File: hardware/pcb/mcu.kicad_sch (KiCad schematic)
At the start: 35 parts, among them J1 Conn_01x05, J2 Conn_01x06, Q1 BC817, SW2 SW_Push, SW3 SW_Push, U2 STM32F411CEU6, U4 PCF8574AP, Y1 8MHz Crystal, Y2 32.768 kHz Crystal

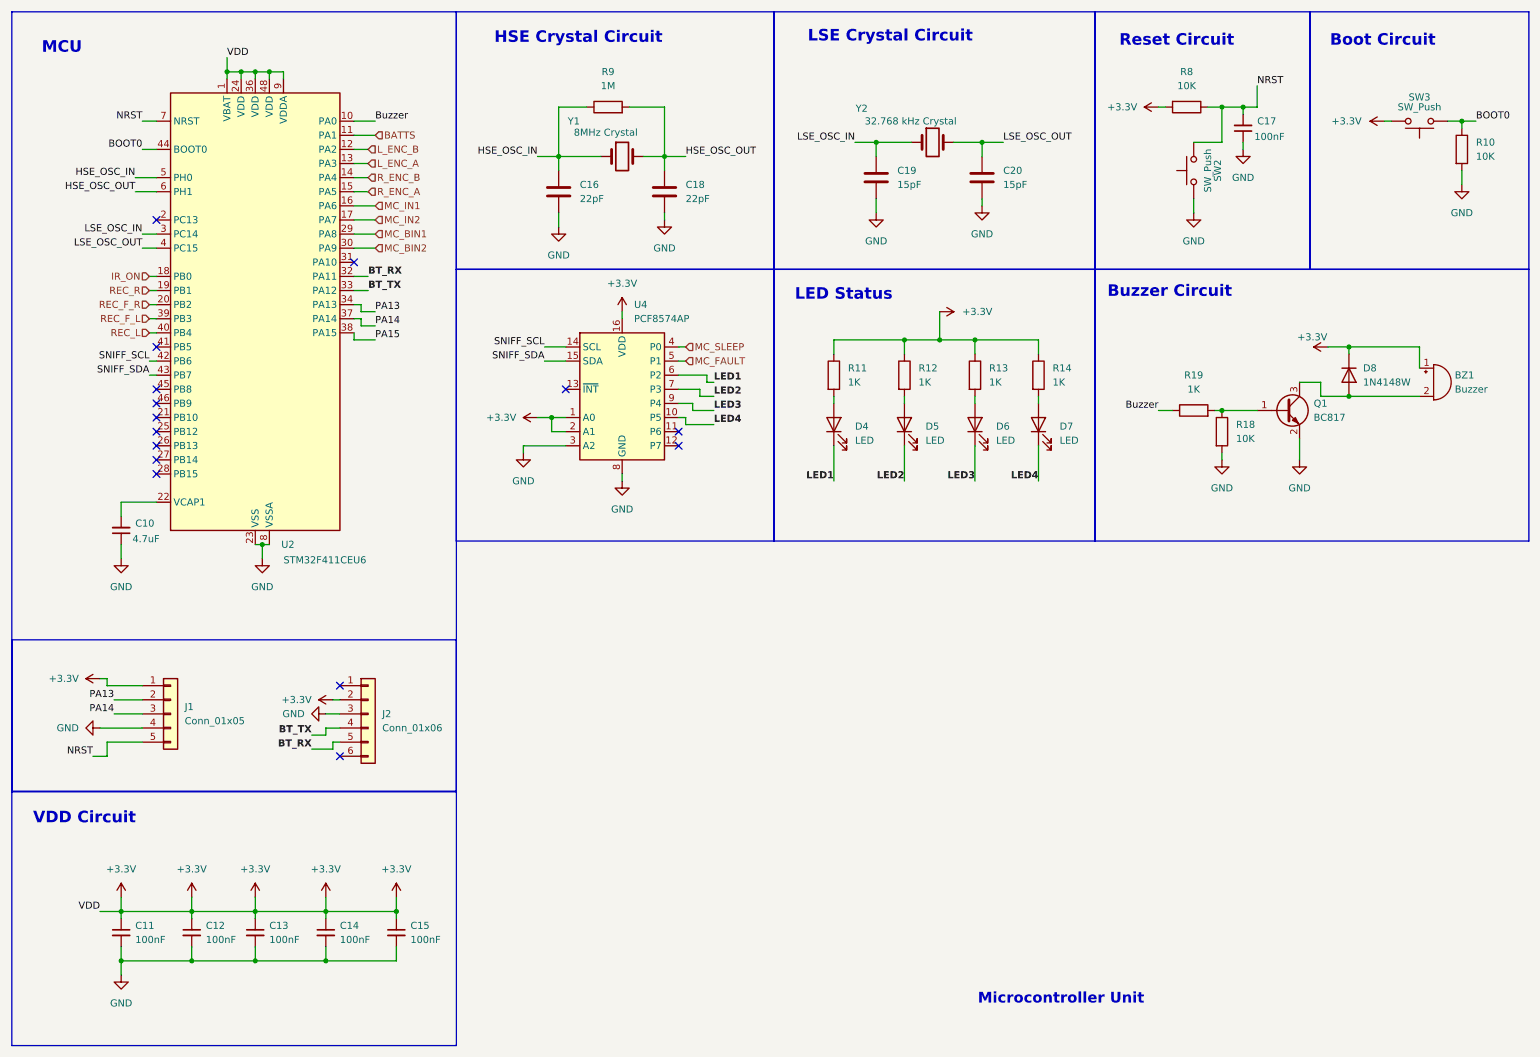
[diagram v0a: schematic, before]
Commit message: hardware: freeze schematic v1 after complete PCB redesign
Complete PCB and schematic refresh with reorganized sheets (psu, ui),
updated MCU/motor/sensor subsystems, and v1 schematic baseline frozen.
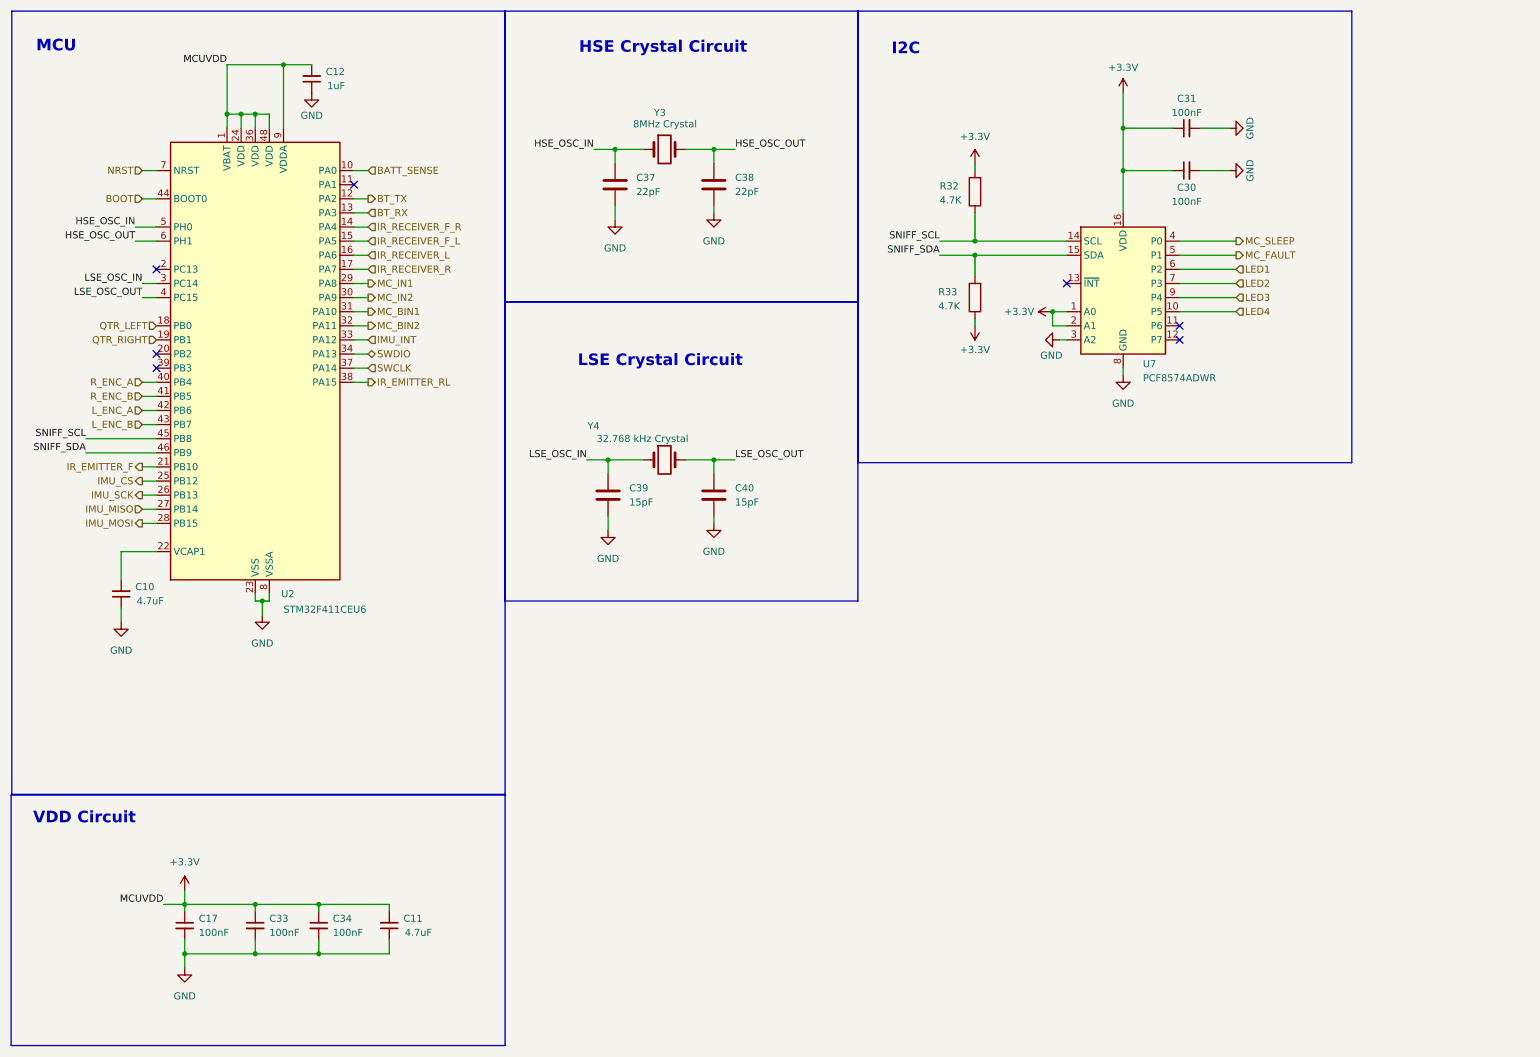
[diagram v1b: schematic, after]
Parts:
- removed BZ1: Buzzer, Buzzer_Beeper:Buzzer_Murata_PKMCS0909E, symbol Device:Buzzer
- removed C13, C14, C15: 100nF, Capacitor_SMD:C_0805_2012Metric_Pad1.18x1.45mm_HandSolder, symbol Device:C_Small
- removed C16, C18: 22pF, Capacitor_SMD:C_0603_1608Metric_Pad1.08x0.95mm_HandSolder, symbol Device:C
- removed C19, C20: 15pF, Capacitor_SMD:C_0603_1608Metric_Pad1.08x0.95mm_HandSolder, symbol Device:C
- removed D4, D5, D6, D7: LED, LED_SMD:LED_0805_2012Metric_Pad1.15x1.40mm_HandSolder, symbol Device:LED
- removed D8: 1N4148W, Diode_SMD:D_SOD-123, symbol Diode:1N4148W
- removed J1: Conn_01x05, Connector_PinHeader_1.00mm:PinHeader_1x05_P1.00mm_Vertical, symbol Connector_Generic:Conn_01x05
- removed J2: Conn_01x06, Connector_PinHeader_1.00mm:PinHeader_1x06_P1.00mm_Vertical, symbol Connector_Generic:Conn_01x06
- removed Q1: BC817, Package_TO_SOT_SMD:SOT-23, symbol Transistor_BJT:BC817
- removed R10, R18, R8: 10K, Resistor_SMD:R_0805_2012Metric_Pad1.20x1.40mm_HandSolder, symbol Device:R
- removed R11, R12, R13, R14, R19: 1K, Resistor_SMD:R_0805_2012Metric_Pad1.20x1.40mm_HandSolder, symbol Device:R
- removed R9: 1M, Resistor_SMD:R_0603_1608Metric_Pad0.98x0.95mm_HandSolder, symbol Device:R
- removed SW2, SW3: SW_Push, Button_Switch_SMD:SW_SPST_B3U-3000P, symbol Switch:SW_Push
- removed U4: PCF8574AP, Package_SO:TSSOP-16_4.4x5mm_P0.65mm, symbol Interface_Expansion:PCF8574AP
- removed Y1: 8MHz Crystal, Crystal:Crystal_SMD_3225-4Pin_3.2x2.5mm_HandSoldering, symbol Device:Crystal
- removed Y2: 32.768 kHz Crystal, Crystal:Crystal_SMD_3225-4Pin_3.2x2.5mm_HandSoldering, symbol Device:Crystal
- added C30, C31, C33, C34: 100nF, Capacitor_SMD:C_0805_2012Metric_Pad1.18x1.45mm_HandSolder, symbol Device:C_Small
- added C37, C38: 22pF, Capacitor_SMD:C_0603_1608Metric_Pad1.08x0.95mm_HandSolder, symbol Device:C
- added C39, C40: 15pF, Capacitor_SMD:C_0603_1608Metric_Pad1.08x0.95mm_HandSolder, symbol Device:C
- added R32, R33: 4.7K, Resistor_SMD:R_0805_2012Metric_Pad1.20x1.40mm_HandSolder, symbol Device:R
- added U7: PCF8574ADWR, Package_SO:SOIC-16W_7.5x10.3mm_P1.27mm, symbol Interface_Expansion:PCF8574AP
- added Y3: 8MHz Crystal, Crystal:Crystal_SMD_3225-4Pin_3.2x2.5mm_HandSoldering, symbol Device:Crystal
- added Y4: 32.768 kHz Crystal, Crystal:Crystal_SMD_3225-4Pin_3.2x2.5mm_HandSoldering, symbol Device:Crystal
- C11: value 100nF -> 4.7uF
- C12: value 100nF -> 1uF
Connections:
- net REC_L is gone; now on net R_ENC_A: U2.40 (PB4)
- net +3.3V: now also C11.2, C12.2, C17.1, C30.1, C31.1, C33.1, C34.1, R32.2, R33.1, U7.1 (A0), U7.16 (VDD), U7.2 (A1); no longer C11.1, C12.1
- net BT_RX: now also U2.13 (PA3); no longer U2.32 (PA11)
- net BT_TX: now also U2.12 (PA2); no longer U2.33 (PA12)
- net GND: now also C11.1, C12.1, C17.2, C30.2, C31.2, C33.2, C34.2, C37.2, C38.2, C39.2, C40.2, U7.3 (A2), U7.8 (GND); no longer C11.2, C12.2, C17.1
- net HSE_OSC_IN: now also C37.1, Y3.1
- net HSE_OSC_OUT: now also C38.1, Y3.2
- net LED1: now also U7.6 (P2)
- net LED2: now also U7.7 (P3)
- net LED3: now also U7.9 (P4)
- net LED4: now also U7.10 (P5)
- net LSE_OSC_IN: now also C39.1, Y4.1
- net LSE_OSC_OUT: now also C40.1, Y4.2
- net L_ENC_A: now also U2.42 (PB6); no longer U2.13 (PA3)
- net L_ENC_B: now also U2.43 (PB7); no longer U2.12 (PA2)
- net MC_BIN1: now also U2.31 (PA10); no longer U2.29 (PA8)
- net MC_BIN2: now also U2.32 (PA11); no longer U2.30 (PA9)
- net MC_FAULT: now also U7.5 (P1)
- net MC_IN1: now also U2.29 (PA8); no longer U2.16 (PA6)
- net MC_IN2: now also U2.30 (PA9); no longer U2.17 (PA7)
- net MC_SLEEP: now also U7.4 (P0)
- net NRST: no longer C17.2
- net R_ENC_A: no longer U2.15 (PA5)
- net R_ENC_B: now also U2.41 (PB5); no longer U2.14 (PA4)
- net SNIFF_SCL: now also U2.45 (PB8), R32.1, U7.14 (SCL); no longer U2.42 (PB6)
- net SNIFF_SDA: now also U2.46 (PB9), R33.2, U7.15 (SDA); no longer U2.43 (PB7)
- net IR_EMITTER_F: now reaches U2.21 (PB10)
- net IMU_CS: now reaches U2.25 (PB12)
- net IMU_SCK: now reaches U2.26 (PB13)
- net IMU_MISO: now reaches U2.27 (PB14)
- net IMU_MOSI: now reaches U2.28 (PB15)
- net BATTS: no longer names the net of U2.11 (PA1)
- net BOOT0 renamed BOOT
- net Buzzer renamed BATT_SENSE
- net IR_ON renamed QTR_LEFT
- net PA13 renamed SWDIO
- net PA14 renamed SWCLK
- net PA15 renamed IR_EMITTER_RL
- net REC_F_L: no longer names the net of U2.39 (PB3)
- net REC_F_R: no longer names the net of U2.20 (PB2)
- net REC_R renamed QTR_RIGHT
- new net IMU_INT: U2.33 (PA12)
- new net IR_RECEIVER_F_L: U2.15 (PA5)
- new net IR_RECEIVER_F_R: U2.14 (PA4)
- new net IR_RECEIVER_L: U2.16 (PA6)
- new net IR_RECEIVER_R: U2.17 (PA7)
- no-connect marks 15 -> 7
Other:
- note added: "I2C"
- note removed: "Boot Circuit"
- note removed: "Buzzer Circuit"
- note removed: "LED Status"
- note removed: "Microcontroller Unit"
- note removed: "Reset Circuit"

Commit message: format öncesi commit
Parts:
- removed C31: 100nF, Capacitor_SMD:C_0805_2012Metric_Pad1.18x1.45mm_HandSolder, symbol Device:C_Small
- removed R32, R33: 4.7K, Resistor_SMD:R_0805_2012Metric_Pad1.20x1.40mm_HandSolder, symbol Device:R
- removed U7: PCF8574ADWR, Package_SO:SOIC-16W_7.5x10.3mm_P1.27mm, symbol Interface_Expansion:PCF8574AP
- added R41, R42: 4.7K, Resistor_SMD:R_0603_1608Metric, symbol Device:R
- added U8: PCA9554PW, PCA9554PW:SOP65P640X120-16N, symbol PCA9554PW:PCA9554PW
- C10, C11: footprint Capacitor_SMD:C_0805_2012Metric_Pad1.18x1.45mm_HandSolder -> Capacitor_SMD:C_0805_2012Metric
- C12, C17, C30, C33, C34: footprint Capacitor_SMD:C_0805_2012Metric_Pad1.18x1.45mm_HandSolder -> Capacitor_SMD:C_0603_1608Metric
- C37, C38, C39, C40: footprint Capacitor_SMD:C_0603_1608Metric_Pad1.08x0.95mm_HandSolder -> Capacitor_SMD:C_0603_1608Metric
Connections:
- net +3.3V: now also C30.2, R41.2, R42.1, U8.16 (VCC); no longer C30.1
- net GND: now also C30.1; no longer C30.2
- net LED1: now also U8.4 (P0)
- net LED2: now also U8.5 (P1)
- net LED3: now also U8.6 (P2)
- net LED4: now also U8.7 (P3)
- net MC_FAULT: now also U8.10 (P5)
- net MC_SLEEP: now also U8.9 (P4)
- net SNIFF_SCL: now also R41.1, U8.14 (SCL)
- net SNIFF_SDA: now also R42.2, U8.15 (SDA)
